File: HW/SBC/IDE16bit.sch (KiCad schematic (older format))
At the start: 13 parts, among them P1 IDE0, U16 74LS32, U17 74LS139, U18 74HC74, U19 74LS08, U20 74LS574, U21 74LS574, U22 74HC245

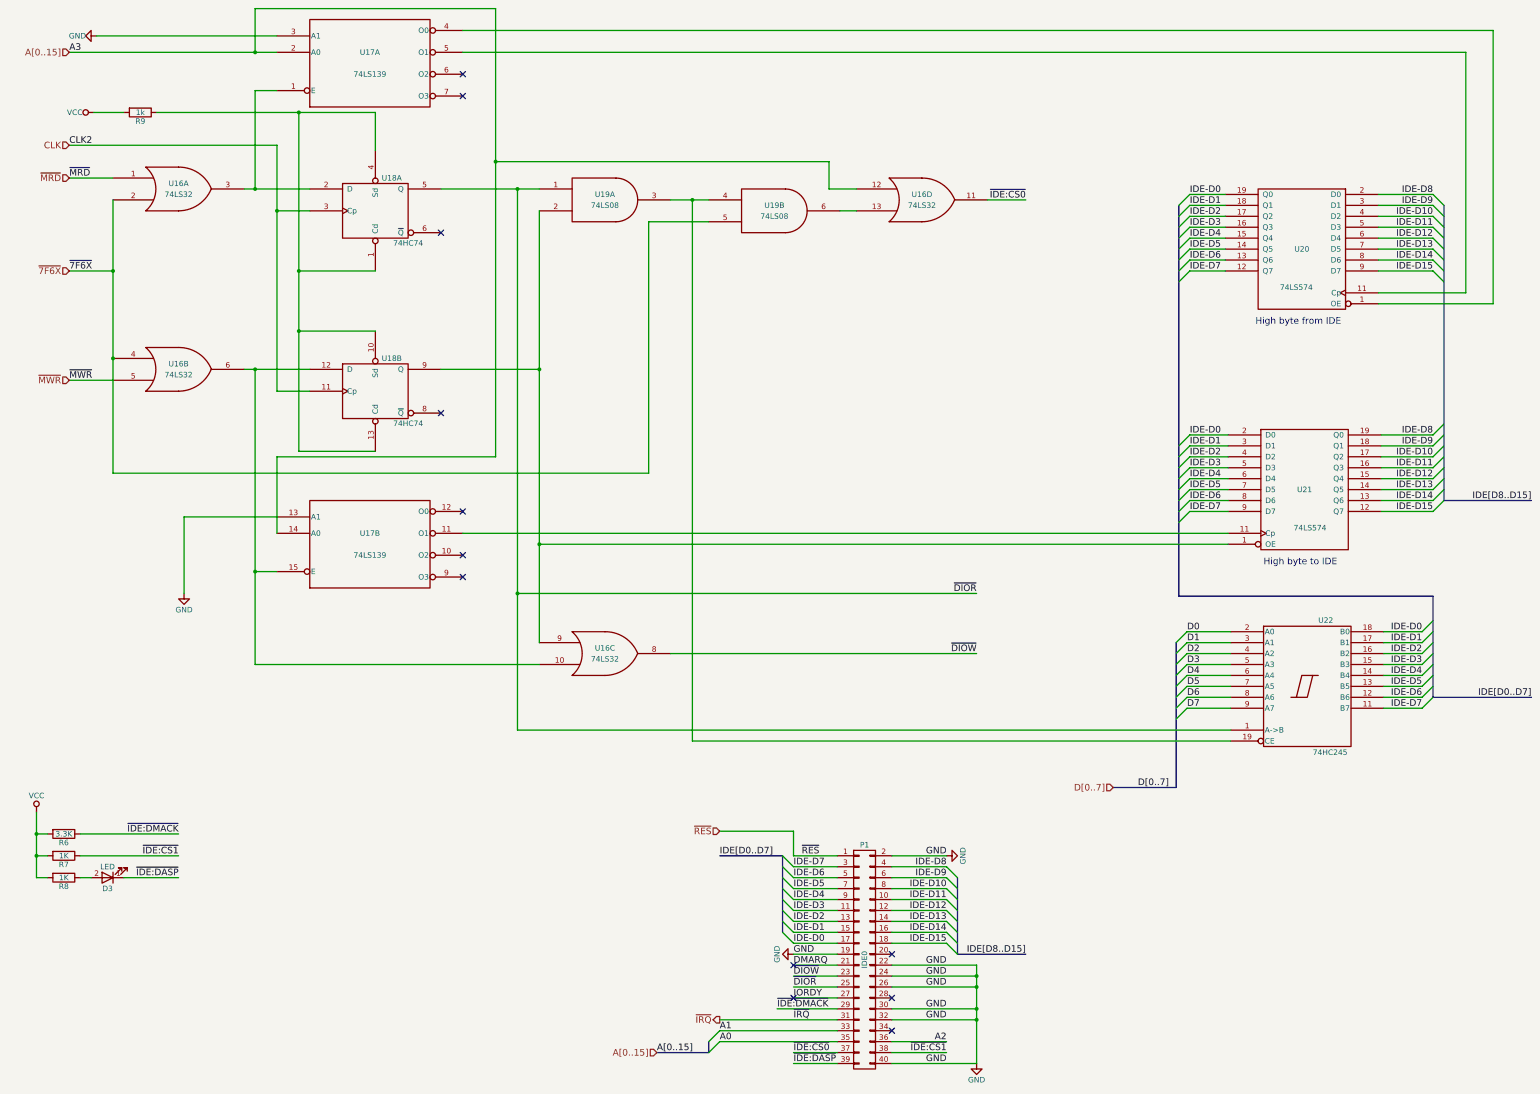
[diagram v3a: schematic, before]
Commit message: Changed all TTLs to HC family.
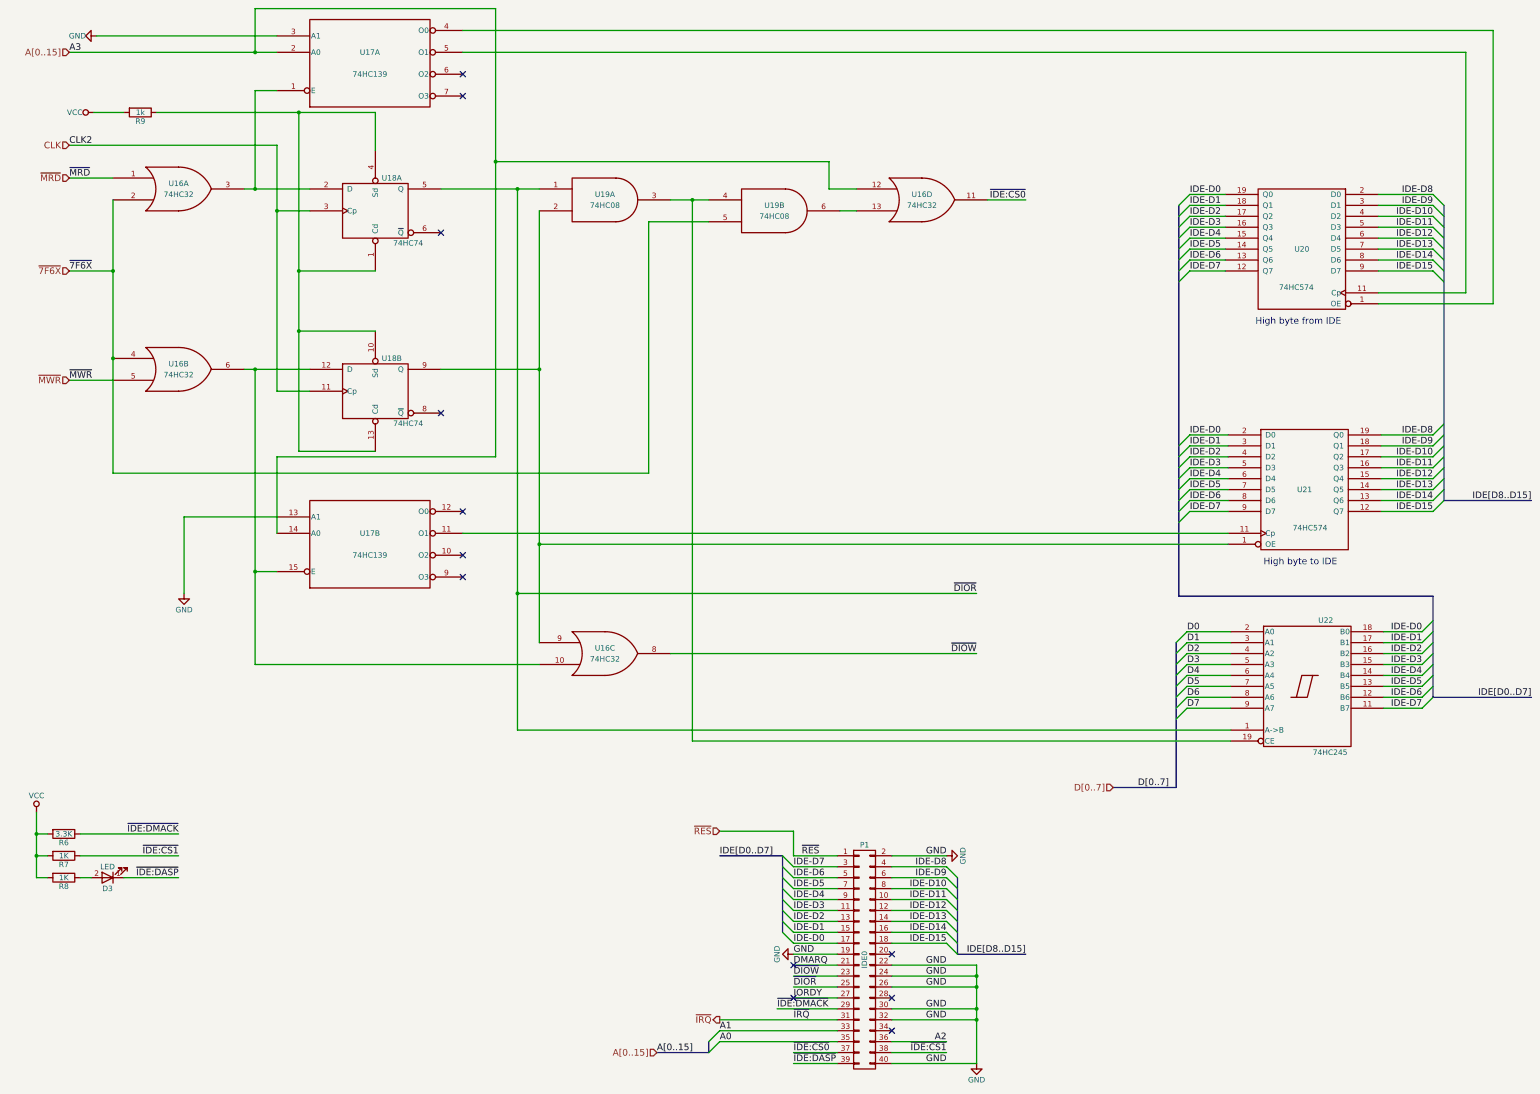
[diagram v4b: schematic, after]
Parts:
- removed U16: 74LS32, Housings_DIP:DIP-14_W7.62mm_Socket, symbol 74LS32
- removed U17: 74LS139, Housings_DIP:DIP-16_W7.62mm_Socket, symbol 74LS139
- removed U19: 74LS08, Housings_DIP:DIP-14_W7.62mm_Socket, symbol 74LS08
- removed U20, U21: 74LS574, Housings_DIP:DIP-20_W7.62mm_Socket, symbol 74LS574
- added U16: 74HC32, symbol 74HC32
- added U17: 74HC139, symbol 74HC139
- added U19: 74HC08, symbol 74HC08
- added U20, U21: 74HC574, symbol 74HC574
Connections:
- net A[0..15]: now also U16.12, U17.14 (A0), U17.2 (A0)
- net GND: now also U16.7 (GND), U16.7 (GND), U16.7 (GND), U16.7 (GND), U17.13 (A1), U17.3 (A1), U17.8 (GND), U17.8 (GND), U19.7 (GND), U19.7 (GND), U20.10 (GND), U21.10 (GND)
- net IDE-D0: now also U20.19 (Q0), U21.2 (D0)
- net IDE-D1: now also U20.18 (Q1), U21.3 (D1)
- net IDE-D10: now also U20.4 (D2), U21.17 (Q2)
- net IDE-D11: now also U20.5 (D3), U21.16 (Q3)
- net IDE-D12: now also U20.6 (D4), U21.15 (Q4)
- net IDE-D13: now also U20.7 (D5), U21.14 (Q5)
- net IDE-D14: now also U20.8 (D6), U21.13 (Q6)
- net IDE-D15: now also U20.9 (D7), U21.12 (Q7)
- net IDE-D2: now also U20.17 (Q2), U21.4 (D2)
- net IDE-D3: now also U20.16 (Q3), U21.5 (D3)
- net IDE-D4: now also U20.15 (Q4), U21.6 (D4)
- net IDE-D5: now also U20.14 (Q5), U21.7 (D5)
- net IDE-D6: now also U20.13 (Q6), U21.8 (D6)
- net IDE-D7: now also U20.12 (Q7), U21.9 (D7)
- net IDE-D8: now also U20.2 (D0), U21.19 (Q0)
- net IDE-D9: now also U20.3 (D1), U21.18 (Q1)
- net VCC: now also U16.14 (VCC), U16.14 (VCC), U16.14 (VCC), U16.14 (VCC), U17.16 (VCC), U17.16 (VCC), U19.14 (VCC), U19.14 (VCC), U20.20 (VCC), U21.20 (VCC)
- net ~7F6X: now also U16.2, U16.4, U19.5
- net ~DIOR: now also U19.1
- net ~DIOW: now also U16.8
- net ~IDE:CS0: now also U16.11
- net ~MRD: now also U16.1
- net ~MWR: now also U16.5
- net at U18.2 (D): now also U16.3, U17.1 (E)
- net at U18.12 (D): now also U16.10, U16.6, U17.15 (E)
- net at U18.9 (Q): now also U16.9, U19.2, U21.1 (OE)
- net at U22.19 (CE): now also U19.3, U19.4
- new net: U17.4 (O0), U20.1 (OE)
- new net: U17.5 (O1), U20.11 (Cp)
- new net: U17.11 (O1), U21.11 (Cp)
- new net: U16.13, U19.6
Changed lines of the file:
@@
-$EndComp
-$Comp
-L 74LS139 U17
-U 1 1 5932FB22
-P 3850 1200
-F 0 "U17" H 3850 1300 50  0000 C CNN
-F 1 "74LS139" H 3850 1100 50  0000 C CNN
-F 2 "Housings_DIP:DIP-16_W7.62mm_Socket" H 3850 1200 50  0001 C CNN
-F 3 "" H 3850 1200 50  0000 C CNN
-	1    3850 1200
-	1    0    0    -1
-$EndComp
-$Comp
-L 74LS139 U17
-U 2 1 5932FB23
-P 3850 5600
-F 0 "U17" H 3850 5700 50  0000 C CNN
-F 1 "74LS139" H 3850 5500 50  0000 C CNN
-F 2 "Housings_DIP:DIP-16_W7.62mm_Socket" H 3850 5600 50  0001 C CNN
-F 3 "" H 3850 5600 50  0000 C CNN
-	2    3850 5600
-	1    0    0    -1
-$EndComp
-$Comp
-L 74LS32 U16
-U 1 1 5932FB24
-P 2100 2350
-F 0 "U16" H 2100 2400 50  0000 C CNN
-F 1 "74LS32" H 2100 2300 50  0000 C CNN
-F 2 "Housings_DIP:DIP-14_W7.62mm_Socket" H 2100 2350 50  0001 C CNN
-F 3 "" H 2100 2350 50  0000 C CNN
-	1    2100 2350
-	1    0    0    -1
-$EndComp
-$Comp
-L 74LS32 U16
-U 2 1 5932FB25
-P 2100 4000
-F 0 "U16" H 2100 4050 50  0000 C CNN
-F 1 "74LS32" H 2100 3950 50  0000 C CNN
-F 2 "Housings_DIP:DIP-14_W7.62mm_Socket" H 2100 4000 50  0001 C CNN
-F 3 "" H 2100 4000 50  0000 C CNN
-	2    2100 4000
-	1    0    0    -1
-$EndComp
-$Comp
-L 74LS32 U16
-U 4 1 5932FB26
-P 8900 2450
-F 0 "U16" H 8900 2500 50  0000 C CNN
-F 1 "74LS32" H 8900 2400 50  0000 C CNN
-F 2 "Housings_DIP:DIP-14_W7.62mm_Socket" H 8900 2450 50  0001 C CNN
-F 3 "" H 8900 2450 50  0000 C CNN
-	4    8900 2450
-	1    0    0    -1
-$EndComp
-$Comp
-L 74LS32 U16
-U 3 1 5932FB27
-P 6000 6600
-F 0 "U16" H 6000 6650 50  0000 C CNN
-F 1 "74LS32" H 6000 6550 50  0000 C CNN
-F 2 "Housings_DIP:DIP-14_W7.62mm_Socket" H 6000 6600 50  0001 C CNN
-F 3 "" H 6000 6600 50  0000 C CNN
-	3    6000 6600
-	1    0    0    -1
-$EndComp
-$Comp
-L 74LS08 U19
-U 2 1 5932FB28
-P 7550 2550
-F 0 "U19" H 7550 2600 50  0000 C CNN
-F 1 "74LS08" H 7550 2500 50  0000 C CNN
-F 2 "Housings_DIP:DIP-14_W7.62mm_Socket" H 7550 2550 50  0001 C CNN
-F 3 "" H 7550 2550 50  0000 C CNN
-	2    7550 2550
-	1    0    0    -1
-$EndComp
-$Comp
-L 74LS574 U20
-U 1 1 5932FB29
-P 12375 2900
-F 0 "U20" H 12375 2900 50  0000 C CNN
-F 1 "74LS574" H 12425 2550 50  0000 C CNN
-F 2 "Housings_DIP:DIP-20_W7.62mm_Socket" H 12375 2900 50  0001 C CNN
-F 3 "" H 12375 2900 50  0000 C CNN
-	1    12375 2900
-	-1   0    0    -1
-$EndComp
-$Comp
-L 74LS574 U21
-U 1 1 5932FB2A
-P 12400 5100
-F 0 "U21" H 12400 5100 50  0000 C CNN
-F 1 "74LS574" H 12450 4750 50  0000 C CNN
-F 2 "Housings_DIP:DIP-20_W7.62mm_Socket" H 12400 5100 50  0001 C CNN
-F 3 "" H 12400 5100 50  0000 C CNN
-	1    12400 5100
-	1    0    0    -1
 $EndComp
 $Comp
@@
 F 3 "" H 800 8050 50  0000 C CNN
 	1    800  8050
-	1    0    0    -1
-$EndComp
-$Comp
-L 74LS08 U19
-U 1 1 5932FB33
-P 6000 2450
-F 0 "U19" H 6000 2500 50  0000 C CNN
-F 1 "74LS08" H 6000 2400 50  0000 C CNN
-F 2 "Housings_DIP:DIP-14_W7.62mm_Socket" H 6000 2450 50  0001 C CNN
-F 3 "" H 6000 2450 50  0000 C CNN
-	1    6000 2450
 	1    0    0    -1
 $EndComp
@@
 	1100 4100 1500 4100
 Wire Wire Line
-	1500 2450 1500 4950
-Wire Wire Line
 	1500 4950 6400 4950
 Wire Wire Line
@@
 	-1   0    0    1
 $EndComp
+$Comp
+L 74HC139 U17
+U 1 1 5A41940B
+P 3850 1200
+F 0 "U17" H 3850 1300 50  0000 C CNN
+F 1 "74HC139" H 3850 1100 50  0000 C CNN
+F 2 "" H 3850 1200 50  0001 C CNN
+F 3 "" H 3850 1200 50  0001 C CNN
+	1    3850 1200
+	1    0    0    -1
+$EndComp
+$Comp
+L 74HC139 U17
+U 2 1 5A419B44
+P 3850 5600
+F 0 "U17" H 3850 5700 50  0000 C CNN
+F 1 "74HC139" H 3850 5500 50  0000 C CNN
+F 2 "" H 3850 5600 50  0001 C CNN
+F 3 "" H 3850 5600 50  0001 C CNN
+	2    3850 5600
+	1    0    0    -1
+$EndComp
+$Comp
+L 74HC32 U16
+U 1 1 5A41A69A
+P 2100 2350
+F 0 "U16" H 2100 2400 50  0000 C CNN
+F 1 "74HC32" H 2100 2300 50  0000 C CNN
+F 2 "" H 2100 2350 50  0001 C CNN
+F 3 "" H 2100 2350 50  0001 C CNN
+	1    2100 2350
+	1    0    0    -1
+$EndComp
+$Comp
+L 74HC32 U16
+U 2 1 5A41AC91
+P 2100 4000
+F 0 "U16" H 2100 4050 50  0000 C CNN
+F 1 "74HC32" H 2100 3950 50  0000 C CNN
+F 2 "" H 2100 4000 50  0001 C CNN
+F 3 "" H 2100 4000 50  0001 C CNN
+	2    2100 4000
+	1    0    0    -1
+$EndComp
+Wire Wire Line
+	1500 2450 1500 4950
+$Comp
+L 74HC32 U16
+U 3 1 5A41CADF
+P 6000 6600
+F 0 "U16" H 6000 6650 50  0000 C CNN
+F 1 "74HC32" H 6000 6550 50  0000 C CNN
+F 2 "" H 6000 6600 50  0001 C CNN
+F 3 "" H 6000 6600 50  0001 C CNN
+	3    6000 6600
+	1    0    0    -1
+$EndComp
+$Comp
+L 74HC32 U16
+U 4 1 5A41D9E7
+P 8900 2450
+F 0 "U16" H 8900 2500 50  0000 C CNN
+F 1 "74HC32" H 8900 2400 50  0000 C CNN
+F 2 "" H 8900 2450 50  0001 C CNN
+F 3 "" H 8900 2450 50  0001 C CNN
+	4    8900 2450
+	1    0    0    -1
+$EndComp
+$Comp
+L 74HC08 U19
+U 1 1 5A41F952
+P 6000 2450
+F 0 "U19" H 6000 2500 50  0000 C CNN
+F 1 "74HC08" H 6000 2400 50  0000 C CNN
+F 2 "" H 6000 2450 50  0001 C CNN
+F 3 "" H 6000 2450 50  0001 C CNN
+	1    6000 2450
+	1    0    0    -1
+$EndComp
+$Comp
+L 74HC08 U19
+U 2 1 5A42066A
+P 7550 2550
+F 0 "U19" H 7550 2600 50  0000 C CNN
+F 1 "74HC08" H 7550 2500 50  0000 C CNN
+F 2 "" H 7550 2550 50  0001 C CNN
+F 3 "" H 7550 2550 50  0001 C CNN
+	2    7550 2550
+	1    0    0    -1
+$EndComp
+$Comp
+L 74HC574 U20
+U 1 1 5A422EB3
+P 12375 2900
+F 0 "U20" H 12375 2900 50  0000 C CNN
+F 1 "74HC574" H 12425 2550 50  0000 C CNN
+F 2 "" H 12375 2900 50  0001 C CNN
+F 3 "" H 12375 2900 50  0001 C CNN
+	1    12375 2900
+	-1   0    0    -1
+$EndComp
+$Comp
+L 74HC574 U21
+U 1 1 5A4236DF
+P 12400 5100
+F 0 "U21" H 12400 5100 50  0000 C CNN
+F 1 "74HC574" H 12450 4750 50  0000 C CNN
+F 2 "" H 12400 5100 50  0001 C CNN
+F 3 "" H 12400 5100 50  0001 C CNN
+	1    12400 5100
+	1    0    0    -1
+$EndComp
 $EndSCHEMATC
